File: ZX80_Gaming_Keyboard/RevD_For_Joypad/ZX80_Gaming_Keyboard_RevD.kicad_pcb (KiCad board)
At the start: 2 copper layers, 185 x 80 mm, 47 parts, among them J1 KB1, J3 KB2, J4 ZX81 Joypad, SW1 1, SW10 E, SW11 D, SW12 X, SW13 4, SW14 R, SW15 F, SW16 C, SW17 5, SW18 T, SW19 G, SW2 Q, SW20 V, SW21 6, SW22 Y, SW23 H, SW24 B, SW25 7, SW26 U, SW27 J, SW28 N, SW29 8, SW3 A, SW30 I, SW31 K, SW32 M, SW33 9, SW34 O, SW35 L, SW36 DOT, SW37 0, SW38 P, SW39 NL, SW4 SHIFT, SW40 SPACE, SW5 2, SW6 W, SW7 S, SW8 Z, SW9 3

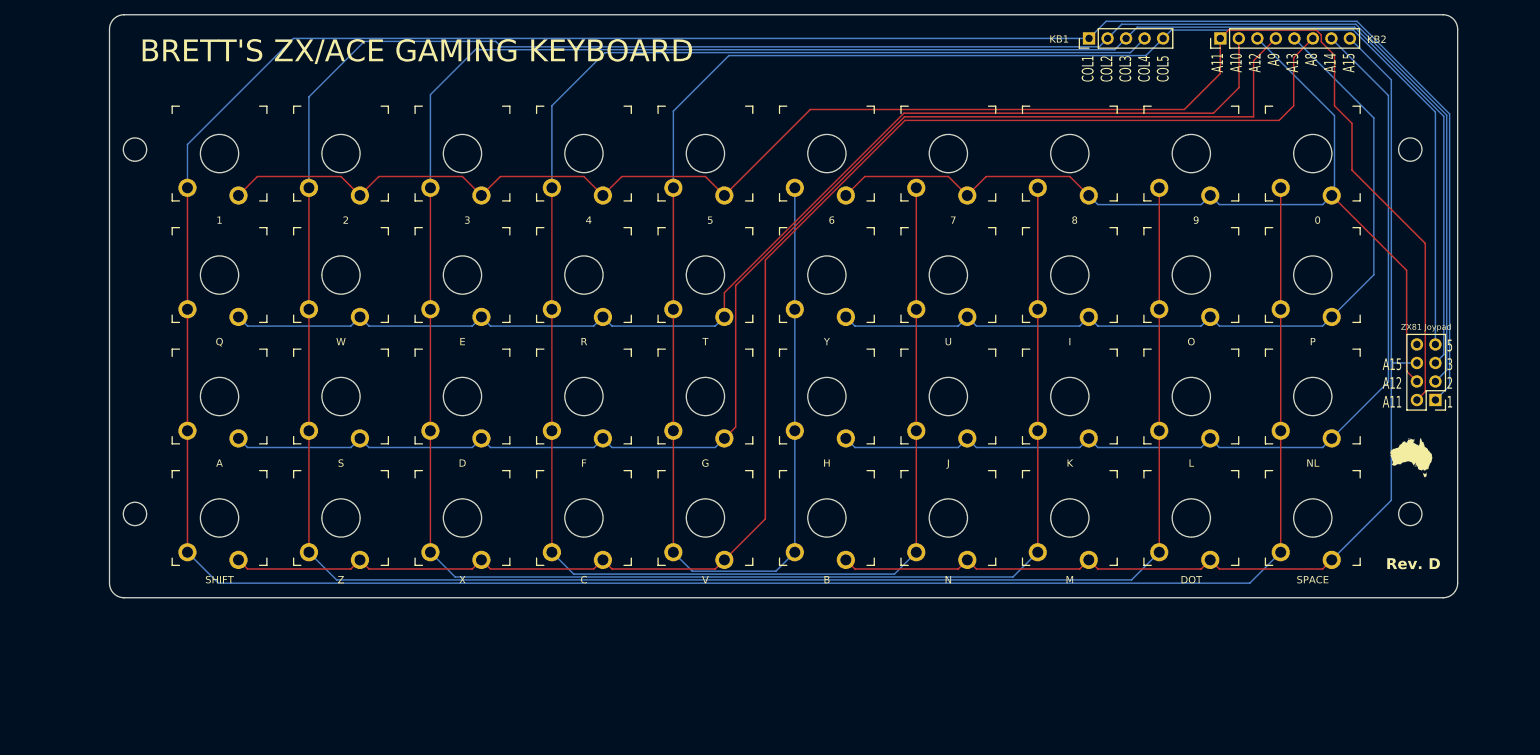
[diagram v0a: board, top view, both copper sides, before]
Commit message: Corrected footprint spacing
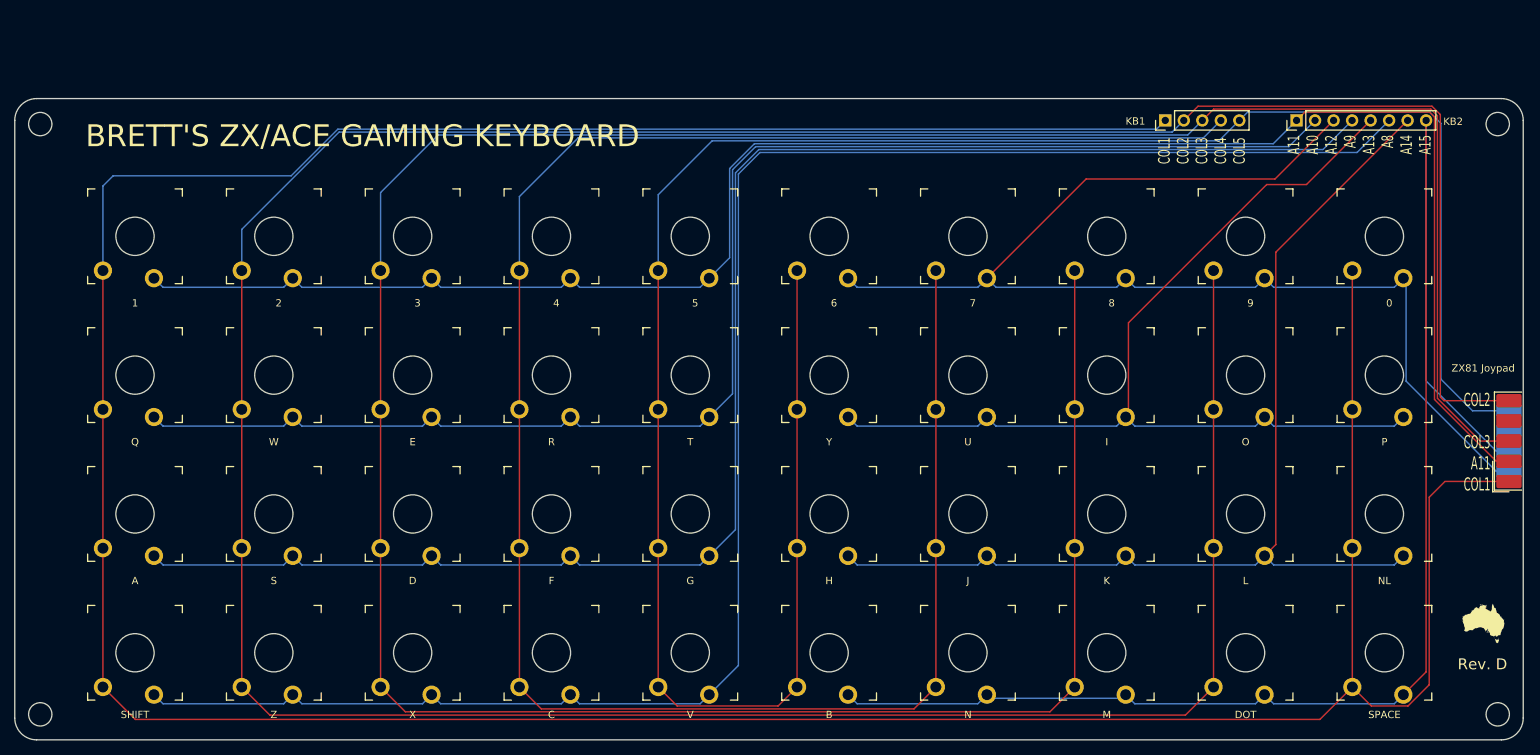
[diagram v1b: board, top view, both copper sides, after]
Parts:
- removed J4: ZX81 Joypad, Connector_PinHeader_2.54mm:PinHeader_2x04_P2.54mm_Vertical
- added J2: ZX81 Joypad, Connector_Dsub:DSUB-9_Pins_EdgeMount_P2.77mm, F.Cu at (272.2, 161.1)
- moved H1 30.4 mm to (70.7, 198.6)
- moved H2 30.0 mm to (270.7, 198.6)
- moved SW4 21.8 mm to (83.7, 190.2)
- moved SW40 20.9 mm to (255.1, 190.2)
- moved SW8 20.7 mm to (102.7, 190.2)
- moved SW36 19.9 mm to (236.1, 190.2)
- moved SW3 19.9 mm to (83.7, 171.1)
- moved SW12 19.7 mm to (121.8, 190.2)
- moved SW32 19.2 mm to (217.0, 190.2)
- moved SW16 19.0 mm to (140.8, 190.2)
- moved SW39 18.9 mm to (255.1, 171.1)
- moved SW28 18.7 mm to (198.0, 190.2)
- moved SW20 18.6 mm to (159.9, 190.2)
- moved SW7 18.6 mm to (102.7, 171.1)
- moved SW24 18.5 mm to (178.9, 190.2)
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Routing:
- net /A15: track 151.7 -> 210.9 mm
- net /COL3: track 381.5 -> 424.2 mm
- net /COL2: track 435.6 -> 476.8 mm
- net /A12: track 129.5 -> 170.4 mm
- net /A8: track 205.9 -> 245.8 mm
- net /A9: track 185.1 -> 222.0 mm
- net /COL4: track 248.9 -> 284.7 mm
- net /A10: track 163.2 -> 198.3 mm
- net /COL5: track 275.1 -> 304.9 mm
- net /A11: track 226.2 -> 249.3 mm
- net /A13: track 115.9 -> 138.2 mm
- net /A14: track 132.2 -> 148.2 mm
- net /COL1: track 485.7 -> 501.0 mm
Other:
- board size 185 x 80 mm -> 207 x 88 mm
- board text added: "Brett Hallen, Jul 2026"
- board text added: "COL2 COL3 A11 COL1"
- board text added: "COL5 A15 A12"
- board text removed: "5 3 2 1"
- board text removed: "A15 A12 A11"
- board text removed: "Brett Hallen, Jun 2026"
